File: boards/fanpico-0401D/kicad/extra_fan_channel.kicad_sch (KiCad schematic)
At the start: 9 parts

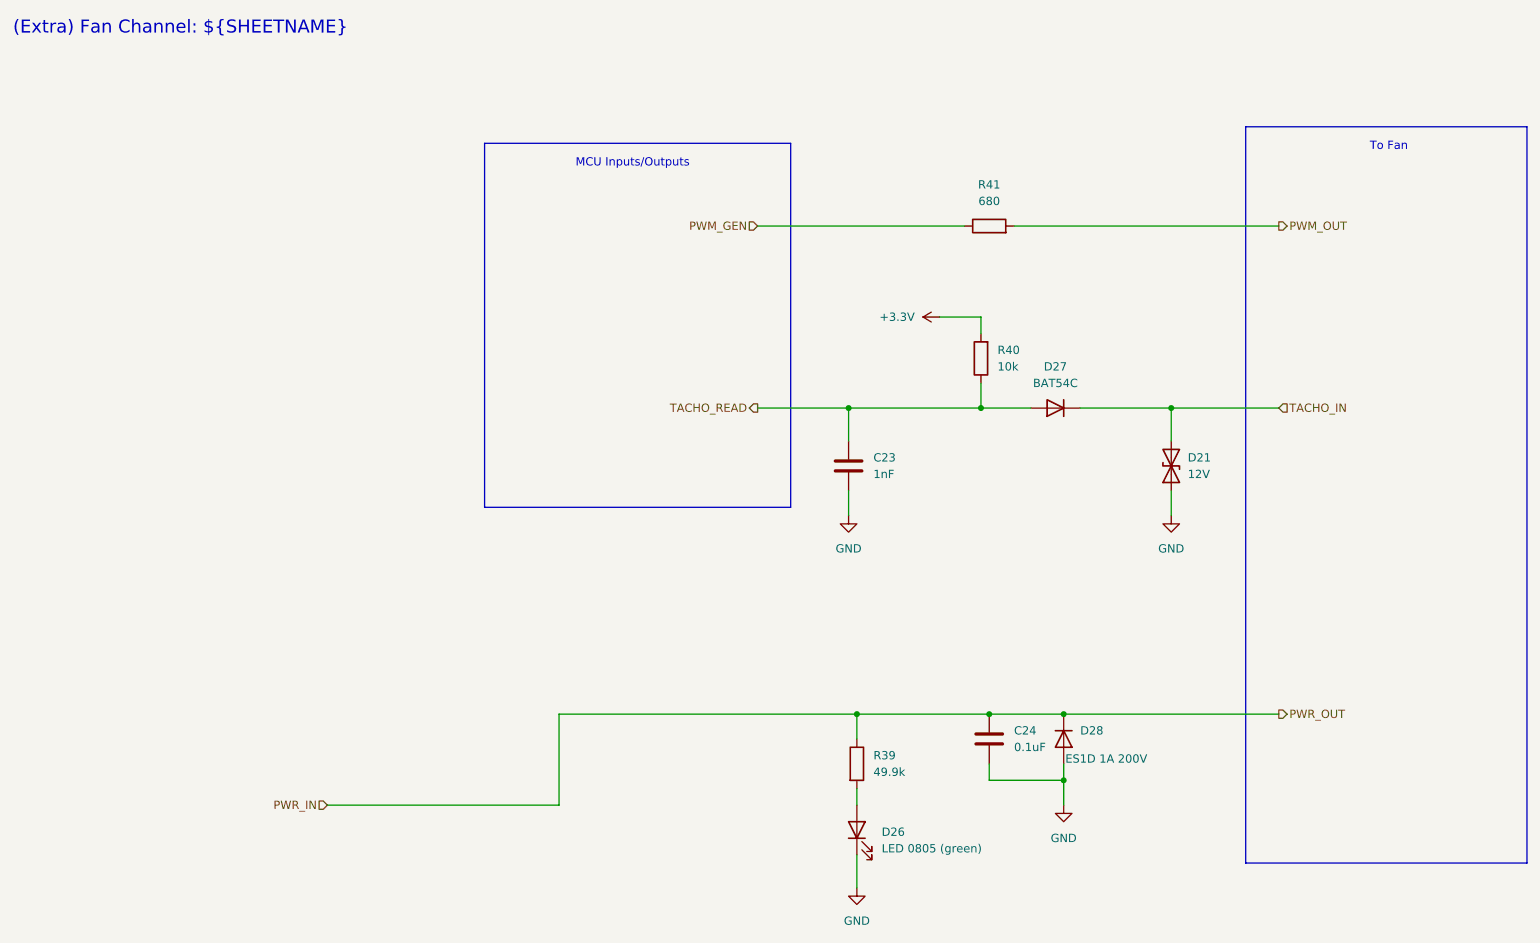
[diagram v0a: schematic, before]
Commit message: Add new 0401D v1.1 PCB (#116)
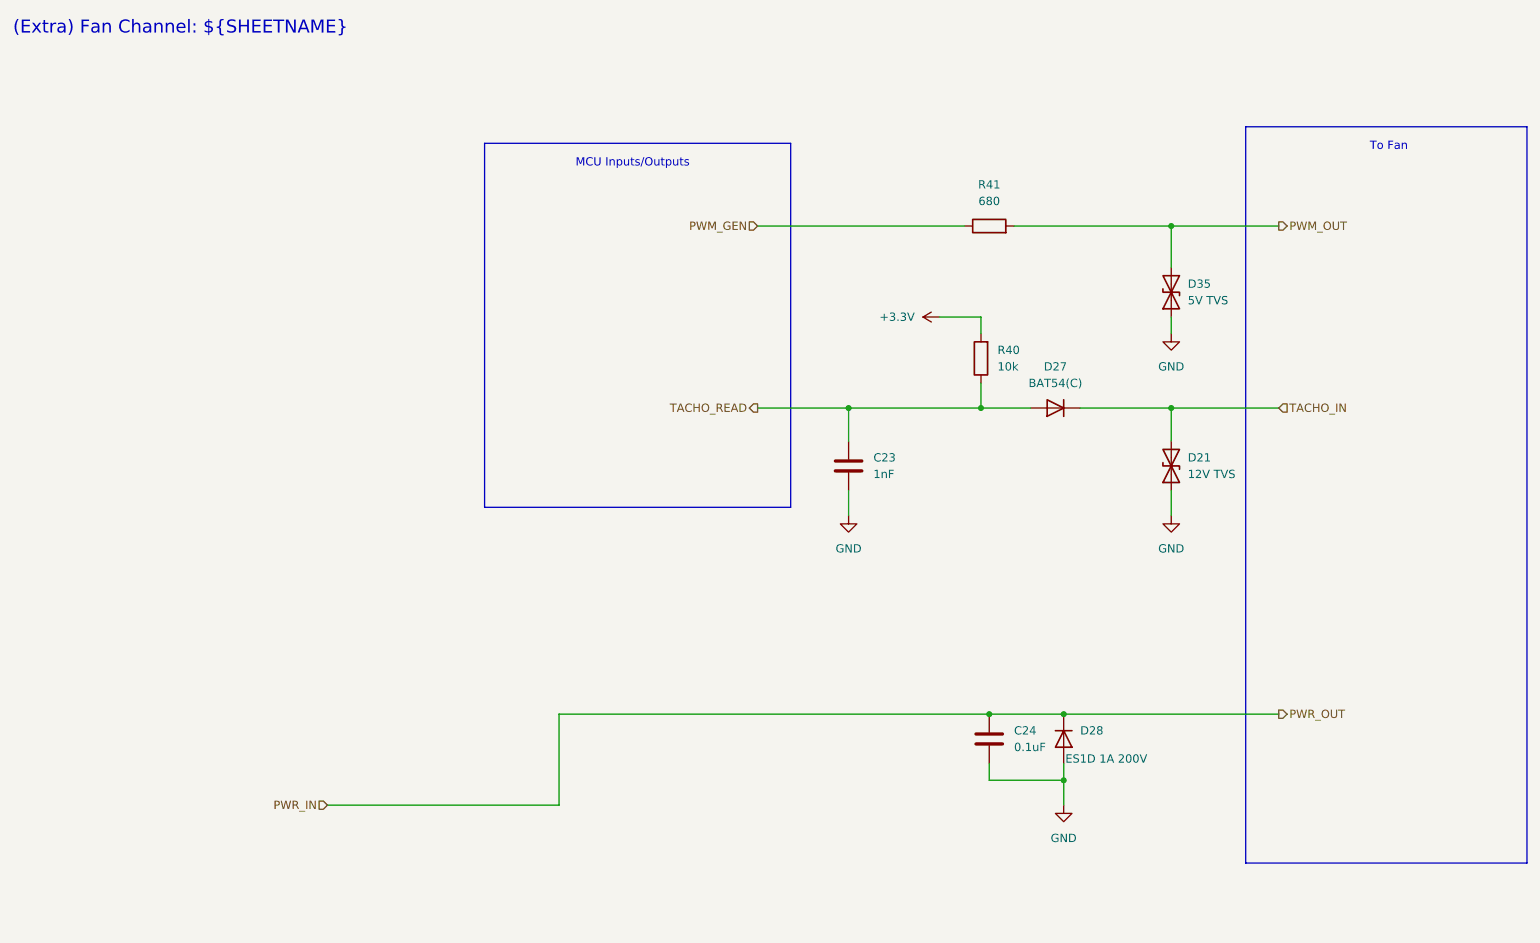
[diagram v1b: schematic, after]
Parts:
- removed D26: LED 0805 (green), LED_SMD:LED_0805_2012Metric_Pad1.15x1.40mm_HandSolder, symbol Device:LED
- removed R39: 49.9k, Resistor_SMD:R_0603_1608Metric_Pad0.98x0.95mm_HandSolder, symbol Device:R
- added D35: 5V TVS, Diode_SMD:D_SOD-323_HandSoldering, symbol Device:D_TVS
- D21: value 12V -> 12V TVS
- D27: value BAT54C -> BAT54(C)
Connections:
- net GND: now also D35.1 (A1)
- net PWM_OUT: now also D35.2 (A2)
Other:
- title: FanPico-0401D v1.0 -> FanPico-0401D v1.1
